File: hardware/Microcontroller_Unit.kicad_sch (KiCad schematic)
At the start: 40 parts, among them U1 W25Q128JVS

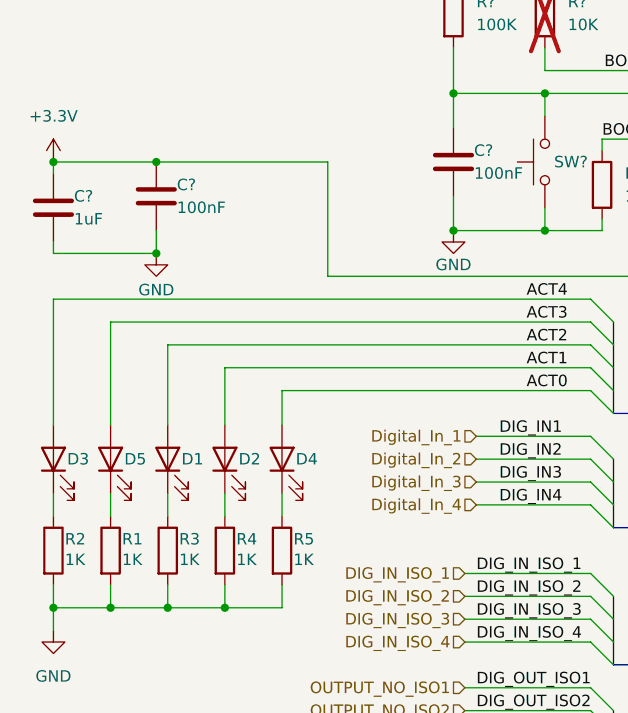
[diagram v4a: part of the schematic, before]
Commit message: Add footprint to components
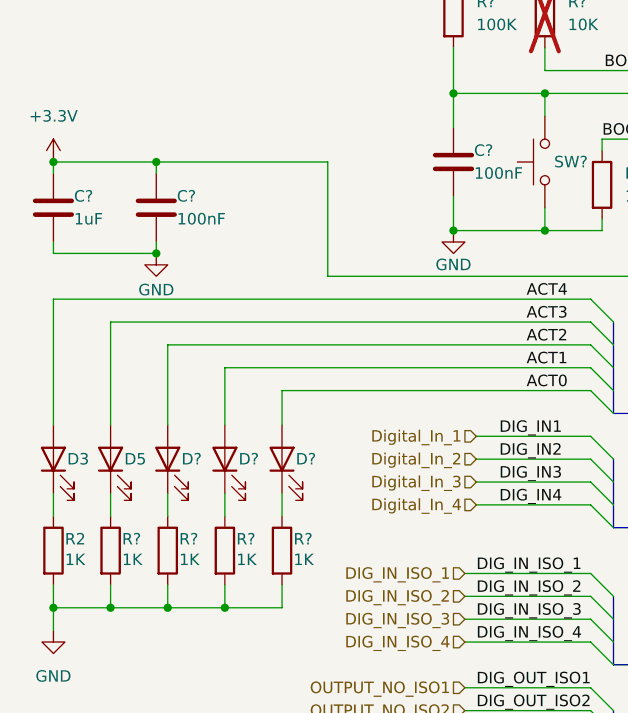
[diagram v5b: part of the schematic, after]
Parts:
- removed D1, D2, D4: LED, LED_SMD:LED_0805_2012Metric_Pad1.15x1.40mm_HandSolder, symbol Device:LED
- removed R1, R3, R4, R5: 1K, Resistor_SMD:R_0805_2012Metric_Pad1.20x1.40mm_HandSolder, symbol Device:R
- added D? (x3): LED, LED_SMD:LED_0603_1608Metric_Pad1.05x0.95mm_HandSolder, symbol Device:LED
- added R? (x4): 1K, Resistor_SMD:R_0603_1608Metric_Pad0.98x0.95mm_HandSolder, symbol Device:R
- C6, C? (x12): footprint Capacitor_SMD:C_0805_2012Metric_Pad1.18x1.45mm_HandSolder -> Capacitor_SMD:C_0603_1608Metric_Pad1.08x0.95mm_HandSolder
- C? (x4): footprint (none) -> Capacitor_SMD:C_0603_1608Metric_Pad1.08x0.95mm_HandSolder
- D3, D5: footprint LED_SMD:LED_0805_2012Metric_Pad1.15x1.40mm_HandSolder -> LED_SMD:LED_0603_1608Metric_Pad1.05x0.95mm_HandSolder
- R2, R6, R? (x2): footprint Resistor_SMD:R_0805_2012Metric_Pad1.20x1.40mm_HandSolder -> Resistor_SMD:R_0603_1608Metric_Pad0.98x0.95mm_HandSolder
- R?: footprint (none) -> Resistor_SMD:R_0603_1608Metric_Pad0.98x0.95mm_HandSolder
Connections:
- net ACT0: now also D?.2 (A)
- net ACT1: now also D?.2 (A)
- net ACT2: now also D?.2 (A)
- net GND: now also R?.2, R?.2, R?.2, R?.2
- net at D5.1 (K): now also R?.1
- new net: D?.1 (K), R?.1 (x3)
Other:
- moved on the sheet: C?

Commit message: Improvements
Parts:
- removed SW?: SW_MEC_5G, symbol Switch:SW_MEC_5G
- removed Y?: 8MHz, symbol Device:Crystal
- removed Y?: 32.768 KHz, symbol Device:Crystal
- added SW1: SW_Push, Button_Switch_SMD:SW_SPST_CK_RS282G05A3, symbol Switch:SW_Push
- added Y1: 8MHz, Crystal:Crystal_SMD_3225-4Pin_3.2x2.5mm, symbol Device:Crystal_GND24
- added Y2: 32.768 KHz, Crystal:Crystal_SMD_3215-2Pin_3.2x1.5mm, symbol Device:Crystal
- C14, C17: renamed from C?; value C -> 22pF
- FB1: renamed from FB?; footprint (none) -> Inductor_SMD:L_0603_1608Metric_Pad1.05x0.95mm_HandSolder
- gave numbers to parts that had none: 28
- renumbered C6 to C29, D3 to D6, D5 to D7, R6 to R11, R2 to R3, U1 to U4
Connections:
- net GND: now also SW1.1, Y1.2 (G), Y1.4 (G)
- net OSC32_IN: now also Y2.1
- net OSC32_OUT: now also Y2.2
- net OSC_IN: now also Y1.1
- net OSC_OUT: now also Y1.3
- net at C19.1, R8.2, U3.14 (NRST): now also SW1.2
- net LAN8720_RESET: now reaches U3.15 (PC0)
- net ESP32_RX: now reaches U3.47 (PB10)
- net ESP32_EN: now reaches U3.55 (PD8)
- net ESP32_TX: now reaches U3.56 (PD9)
- net OUTPUT_NO_ISO1: no longer names the net of U3.81 (PD0)
- net OUTPUT_NO_ISO1: no longer U3.90 (PB4)
- net OUTPUT_NO_ISO2: no longer names the net of U3.82 (PD1)
- net OUTPUT_NO_ISO2: no longer U3.91 (PB5)
- net OUTPUT_NO_ISO3: no longer names the net of U3.83 (PD2)
- net OUTPUT_NO_ISO3: no longer U3.92 (PB6)
- net OUTPUT_NO_ISO4: no longer names the net of U3.84 (PD3)
- net OUTPUT_NO_ISO4: no longer U3.93 (PB7)
- no-connect marks 28 -> 32

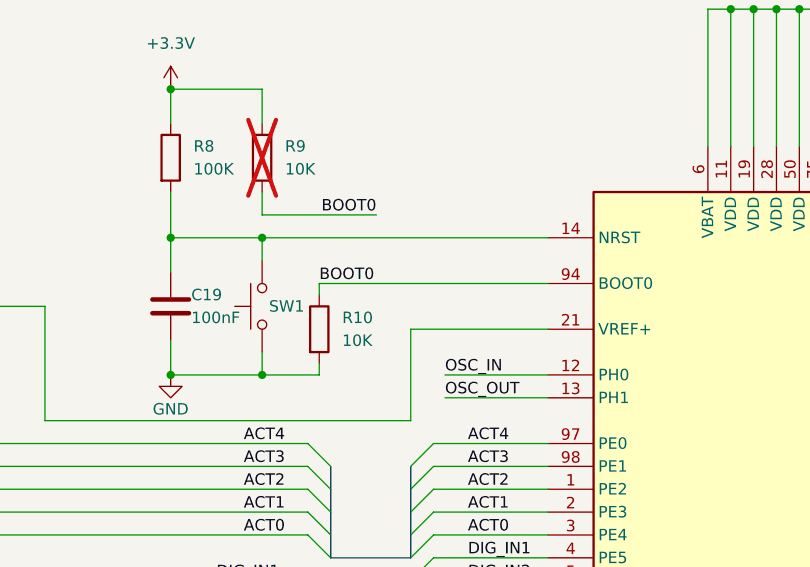
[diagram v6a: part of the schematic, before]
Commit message: Make connectors DB9
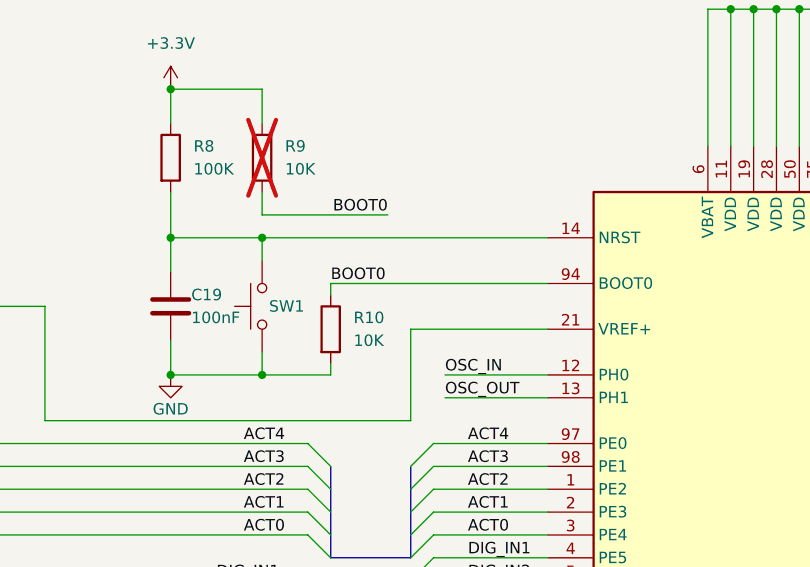
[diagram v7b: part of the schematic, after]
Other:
- moved on the sheet: R10
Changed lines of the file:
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@@
 	(wire
 		(pts
-			(xy 85.09 41.91) (xy 72.39 41.91)
+			(xy 86.36 41.91) (xy 72.39 41.91)
 		)
 		(stroke
@@
 	(wire
 		(pts
+			(xy 72.39 39.37) (xy 72.39 41.91)
+		)
+		(stroke
+			(width 0)
+			(type default)
+		)
+	)
+	(wire
+		(pts
 			(xy 88.9 153.67) (xy 88.9 160.02)
 		)
@@
 	(wire
 		(pts
-			(xy 78.74 50.8) (xy 78.74 49.53)
+			(xy 80.01 50.8) (xy 80.01 49.53)
 		)
 		(stroke
@@
 	(wire
 		(pts
-			(xy 72.39 59.69) (xy 78.74 59.69)
-		)
-		(stroke
-			(width 0)
-			(type default)
-		)
-	)
-	(wire
-		(pts
-			(xy 72.39 41.91) (xy 72.39 39.37)
+			(xy 72.39 59.69) (xy 80.01 59.69)
 		)
 		(stroke
@@
 	(wire
 		(pts
-			(xy 78.74 49.53) (xy 104.14 49.53)
+			(xy 80.01 49.53) (xy 104.14 49.53)
 		)
 		(stroke
@@
 	(wire
 		(pts
-			(xy 78.74 59.69) (xy 78.74 58.42)
+			(xy 80.01 59.69) (xy 80.01 58.42)
 		)
 		(stroke
@@
 	)
 	(label "BOOT0"
-		(at 85.09 41.91 180)
+		(at 86.36 41.91 180)
 		(effects
 			(font
@@
 	)
 	(label "BOOT0"
-		(at 78.74 49.53 0)
+		(at 80.01 49.53 0)
 		(effects
 			(font
@@
 	(symbol
 		(lib_id "Device:R")
-		(at 78.74 54.61 0)
+		(at 80.01 54.61 0)
 		(unit 1)
 		(exclude_from_sim no)
@@
 		(fields_autoplaced yes)
 		(property "Reference" "R10"
-			(at 81.28 53.3399 0)
+			(at 82.55 53.3399 0)
 			(effects
 				(font
@@
 		)
 		(property "Value" "10K"
-			(at 81.28 55.8799 0)
+			(at 82.55 55.8799 0)
 			(effects
 				(font
@@
 		)
 		(property "Footprint" "Resistor_SMD:R_0603_1608Metric_Pad0.98x0.95mm_HandSolder"
-			(at 76.962 54.61 90)
+			(at 78.232 54.61 90)
 			(effects
 				(font
@@
 		)
 		(property "Datasheet" "~"
-			(at 78.74 54.61 0)
+			(at 80.01 54.61 0)
 			(effects
 				(font
@@
 		)
 		(property "Description" "Resistor"
-			(at 78.74 54.61 0)
+			(at 80.01 54.61 0)
 			(effects
 				(font

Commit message: Improvements
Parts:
- added J26: Conn_01x07, Connector_Harwin:Harwin_M20-89007xx_1x07_P2.54mm_Horizontal, symbol Connector_Generic:Conn_01x07
- SW1: now not fitted
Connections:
- net +3.3V: now also J26.1 (Pin_1)
- net BOOT0: now also J26.4 (Pin_4)
- net GND: now also J26.2 (Pin_2)
- net OUTPUT_ISO1: now also U3.92 (PB6); no longer U3.35 (PB0)
- net OUTPUT_ISO2: now also U3.93 (PB7); no longer U3.36 (PB1)
- net OUTPUT_ISO3: now also U3.95 (PB8); no longer U3.37 (PB2)
- net OUTPUT_ISO4: now also U3.96 (PB9); no longer U3.89 (PB3)
- net MCU_RESET: now reaches C19.1, R8.2, SW1.2, U3.14 (NRST)
- net MCU_RESET: now also J26.3 (Pin_3)
- net SWDIO: now reaches U3.72 (PA13)
- net SWDIO: now also J26.5 (Pin_5)
- net SWCLK: now reaches U3.76 (PA14)
- net SWCLK: now also J26.6 (Pin_6)
- new net SWO: J26.7 (Pin_7), U3.89 (PB3)
- no-connect marks 32 -> 29
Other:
- note added: "Programmign Header"
- moved on the sheet: C14, C15, C17, C18, Y1, Y2
